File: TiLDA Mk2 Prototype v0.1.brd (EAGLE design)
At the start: 68 x 100 mm, 213 parts, among them IC1 ATSAM3X8EA-AU, IC2 MPU-6050, IC3 SRF-V1.2, IC4 LTC4160, IC5 S25FL216K0PMFI011, IC6 AT45DB161E-SSHFHA (NP), IC7 HMC5883LSMD (NP), IC8 MCP1825T-3302E/DC, J1 FCI 62684-401100ALF, J2 EPD-62684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

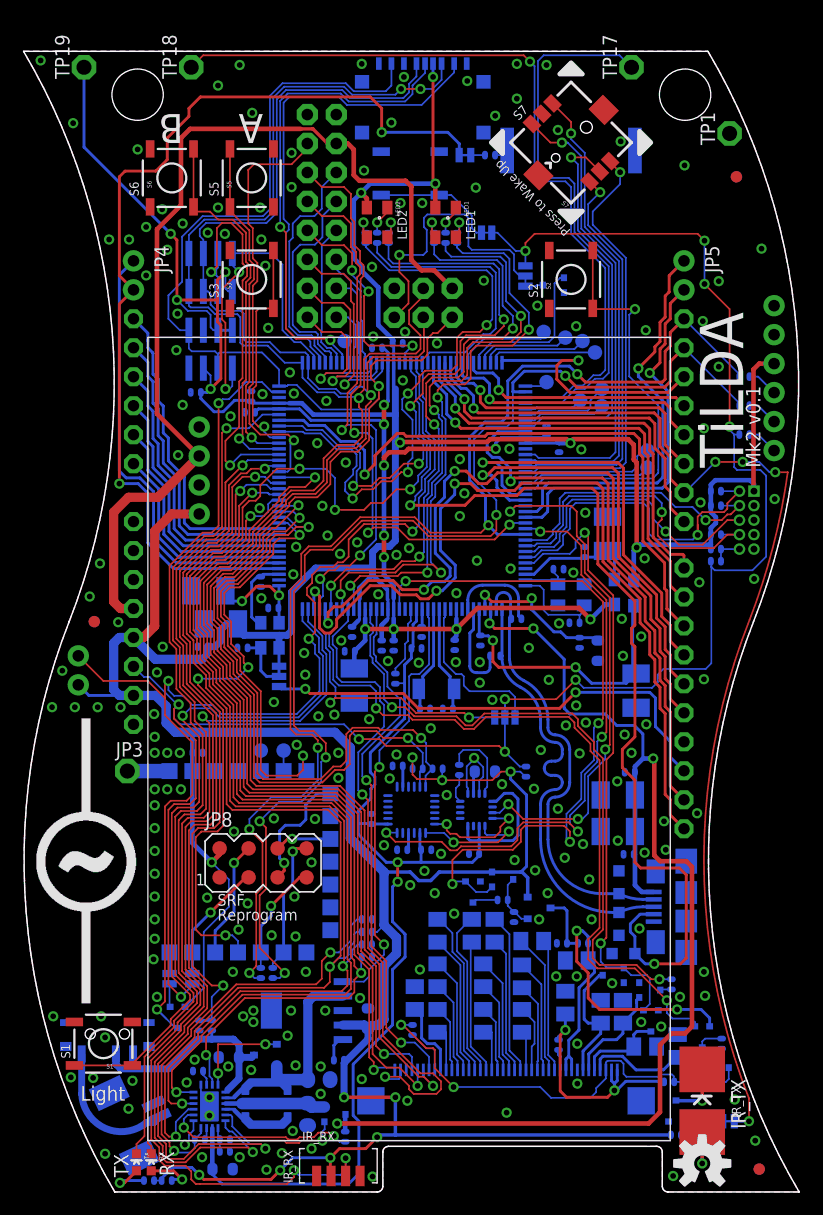
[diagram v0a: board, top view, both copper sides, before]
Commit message: Prototype: Lots of cleaning up, part values, few tracks, Added decoupling for IR TX and FTDI
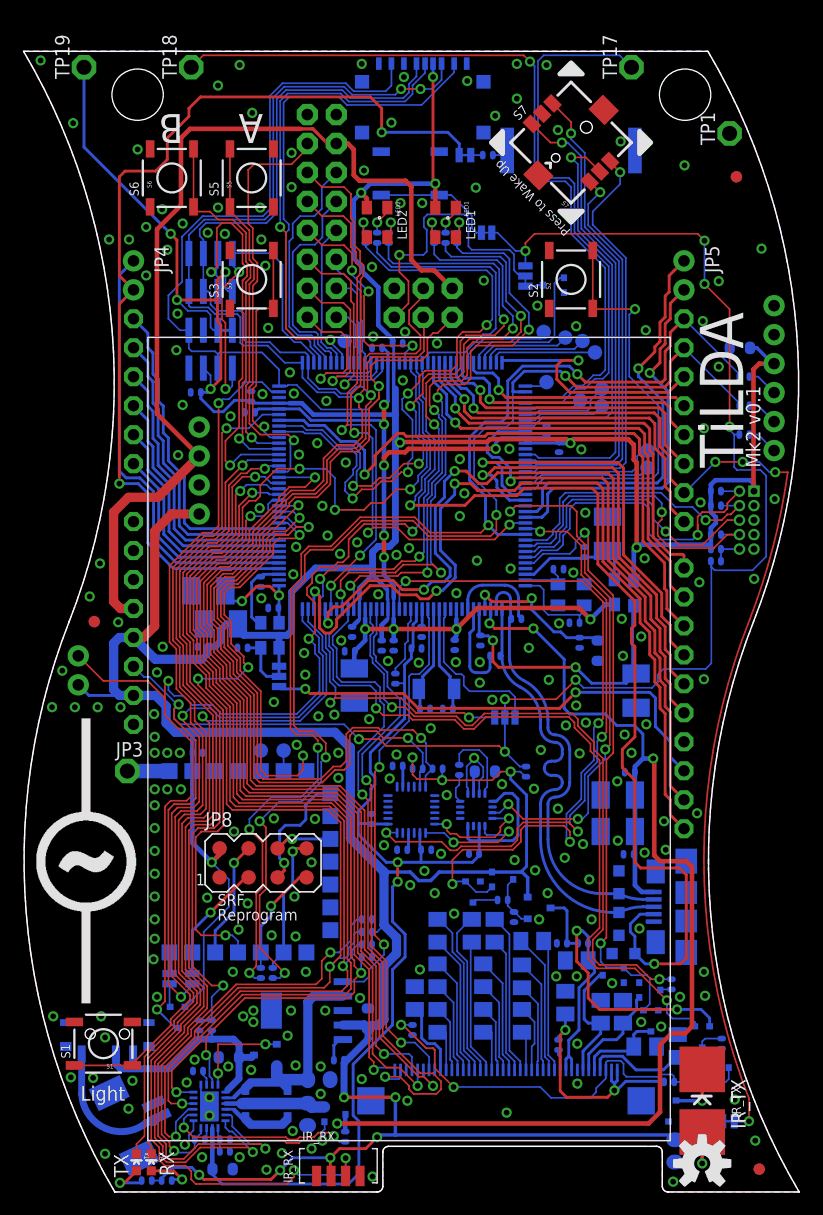
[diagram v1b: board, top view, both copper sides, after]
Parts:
- removed U$2: BATTERY-OUTLINE-55X44, TiLDA Mk2 Parts:BATTERY-55X44
- added C37: 0805/22u/25V/X5R, TiLDA Mk2 Parts:C0805RND
- added C38: 0603/1u/6V/X5R, TiLDA Mk2 Parts:C0603-ROUND
- added OUTINE2: BATTERY-OUTLINE32X50-52X64, TiLDA Mk2 Parts:BATTERY-32X50-52X64
- C104, C105, C106, C107, C108, C109, C110, C112, C113, C114, C115, C116, C117, C118, C119, C132, C134, C2, C27, C29, C32, C9: value 0402/100n/10V/Y5V -> 0402/100n/10V/X5R
- C120: value 0402/10n/10v -> 0402/10n/10v/Y5V
- C22: value 0805/2.2u/25v/y5v -> 0805/2.2u/25V/Y5V
- C26: value 0402/100n/16V/X7R -> 0402/100n/10V/X5R
- C3: value 0402/100n/16V/Y5V -> 0402/100n/10V/X5R
- C31: value 0402/u22/10V/X5R -> 0402/0u22/10V/X5R
- C4: value 0402/100n/4V/X7R -> 0402/100n/10V/X5R
- C6: value 0402/100n/2V/X7R -> 0402/100n/10V/X5R
- J1: value FCI 62684-401100ALF -> ZX62-AB-5PA(11)
- J2: value EPD-62684 -> FCI 62684-401100ALF
- J3: value ARDUINOSPI-REFRENCE -> Arduino Headers
- J5: value 1050270001 -> 1050270001 (NP)
- JP2: value JTAG -> JTAG M50-3500542
- Q12: value FDMA905P -> SI2333DS-T1-E3
- Q8: value BC847BSDM?? -> BSS84W
- R10, R21, R22, R23, R24: value 0402/100K/5% -> 0402/100K/1%
- R102: value 0402/10K -> 0402/10K/5%
- R104: value 0402/100K -> 0402/100K/1%
- R2: value 0402/33K/5%/(NC) -> 0402/33K/5%/(NP)
- R3: value 0402/0R/5%/(NC) -> 0402/0R/5%/(NP)
- RX: value 0603//LED/RED -> 0603/LED/RED
- S1: value Light -> SKQGAKE010
- S2: value Left -> SKQGAKE010
- S3: value Right -> SKQGAKE010
- S4: value Reset -> SKQGAKE010
- S5: value A -> SKQGAKE010
- S6: value B -> SKQGAKE010
- S7: value JOYSTICK_MINI-APLS -> SKRHAAE010
- moved R4 1.80 mm to (59.0, 5.00)
- moved R8 0.20 mm to (10.8, 1.00)
- moved R25 0.20 mm to (40.7, 90.9)
- renumbered U1 to OUTLINE3, U5 to OUTLINE1
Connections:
- net 3V3: now also C37.1, C38.2
- net GND: now also C37.2, C38.1
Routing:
- net 3V3: track 455.5 -> 460.6 mm
- net IR_TX_A: track 6.81 -> 5.31 mm
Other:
- board text added: "C37"
- board text added: "C38"

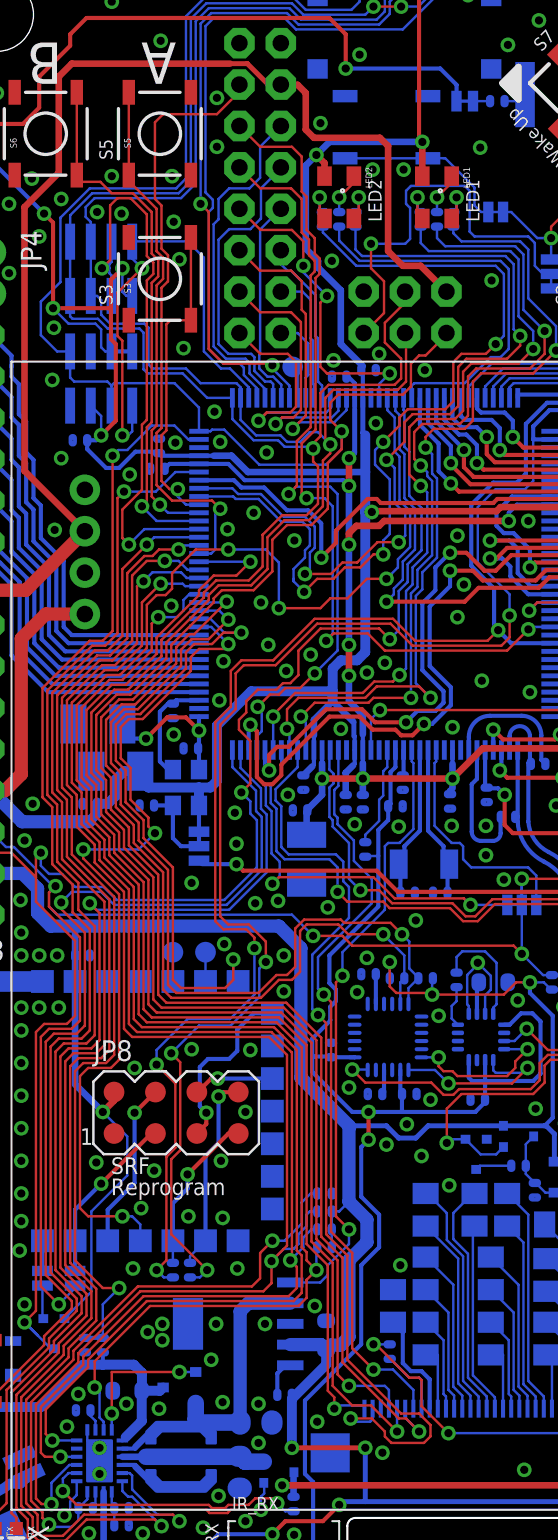
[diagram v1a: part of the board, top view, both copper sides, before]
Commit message: Prototype: swap C30 & C35 for 0805
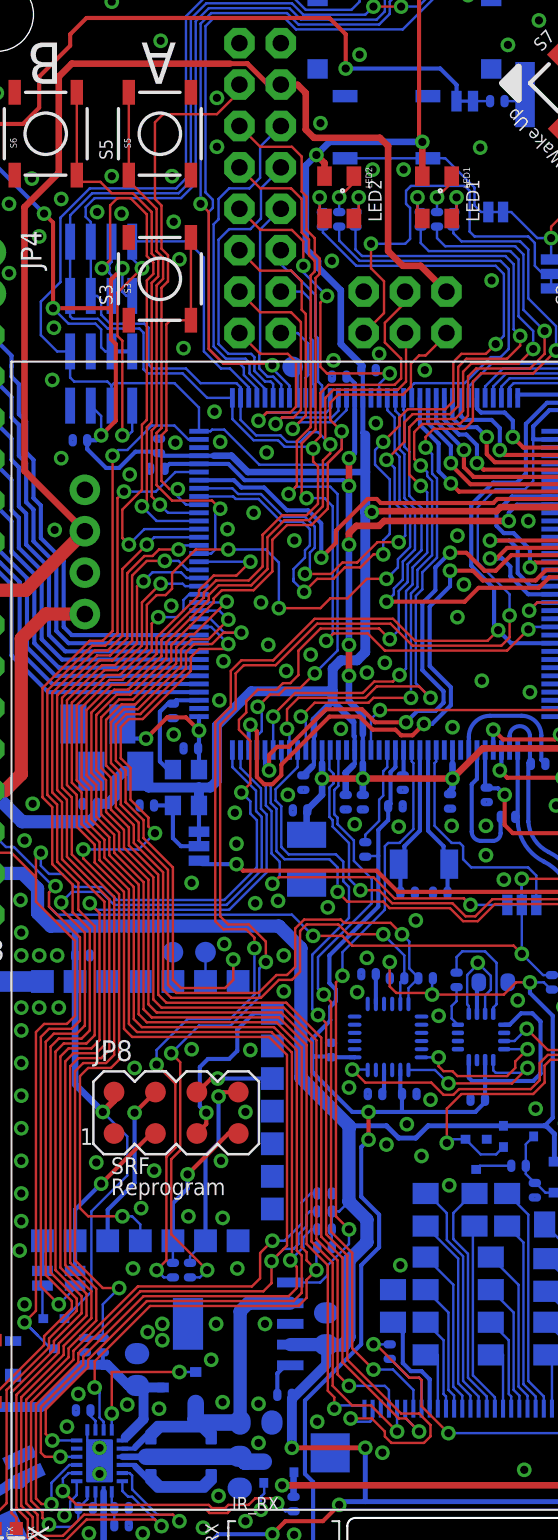
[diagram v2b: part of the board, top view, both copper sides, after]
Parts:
- C30, C35: value 0603/10u/6.3V/X5R -> 0805/10u/6.3V/X5R; device TiLDA Mk2 Parts:C0603-ROUND -> TiLDA Mk2 Parts:C0805RND
- moved C35 1.43 mm to (18.6, 13.1), turned to 270 degrees
- moved C30 0.40 mm to (30.2, 15.6)
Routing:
- net VBATT_SWITCHED: track 19.9 -> 19.4 mm
- net GND: vias 236 -> 235
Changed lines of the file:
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@@
 <setting verticaltext="up"/>
 </settings>
-<grid distance="0.5" unitdist="mm" unit="mm" style="lines" multiple="1" display="yes" altdistance="0.25" altunitdist="mm" altunit="mm"/>
+<grid distance="0.1" unitdist="mm" unit="mm" style="lines" multiple="1" display="yes" altdistance="0.05" altunitdist="mm" altunit="mm"/>
 <layers>
 <layer number="1" name="Top" color="4" fill="1" visible="yes" active="yes"/>
@@
 <layer number="38" name="bTest" color="7" fill="1" visible="no" active="yes"/>
 <layer number="39" name="tKeepout" color="4" fill="11" visible="no" active="yes"/>
-<layer number="40" name="bKeepout" color="1" fill="11" visible="yes" active="yes"/>
+<layer number="40" name="bKeepout" color="1" fill="11" visible="no" active="yes"/>
 <layer number="41" name="tRestrict" color="4" fill="10" visible="no" active="yes"/>
 <layer number="42" name="bRestrict" color="1" fill="10" visible="no" active="yes"/>
@@
 <text x="27.95" y="96.6" size="0.8128" layer="22" ratio="15" rot="MR90">J5</text>
 <text x="10" y="38.2" size="0.8128" layer="22" ratio="15" rot="MR0">ANT</text>
-<text x="19.5" y="12.6" size="0.8128" layer="22" ratio="15" rot="MR90">Q12</text>
+<text x="19.5" y="12.5" size="0.8128" layer="22" ratio="15" rot="MR90">Q12</text>
 <text x="29" y="3.2" size="0.8128" layer="22" ratio="15" rot="MR90">Q11</text>
 <text x="59.7" y="6.6" size="0.8128" layer="22" ratio="15" rot="MR0">Q9</text>
@@
 <text x="20.9" y="1.1" size="0.6096" layer="22" ratio="15" rot="MR0">C34</text>
 <text x="15.4" y="11.9" size="0.6096" layer="22" ratio="15" rot="MR0">R29</text>
-<text x="18.9" y="12.6" size="0.6096" layer="22" ratio="15" rot="MR0">C35</text>
+<text x="17" y="12" size="0.6096" layer="22" ratio="15" rot="MR90">C35</text>
 <text x="24.4" y="3.2" size="0.6096" layer="22" ratio="15" rot="MR90">C33</text>
 <text x="30" y="2.7" size="0.6096" layer="22" ratio="15" rot="MR90">R28</text>
@@
 <text x="26.5" y="10.7" size="0.6096" layer="22" ratio="15" rot="MR0">C36</text>
 <text x="31.1" y="14.4" size="0.6096" layer="22" ratio="15" rot="MR90">C30</text>
-<text x="17.9" y="13.9" size="0.6096" layer="22" ratio="15" rot="MR90">R38</text>
-<text x="17.1" y="13.9" size="0.6096" layer="22" ratio="15" rot="MR90">R39</text>
+<text x="18" y="15.6" size="0.6096" layer="22" ratio="15" rot="MR90">R38</text>
+<text x="17.2" y="15.6" size="0.6096" layer="22" ratio="15" rot="MR90">R39</text>
 <text x="19.8" y="17.3" size="0.6096" layer="22" ratio="15" rot="MR90">R6</text>
 <text x="19" y="17.3" size="0.6096" layer="22" ratio="15" rot="MR90">R5</text>
@@
 <element name="L1" library="TiLDA Mk2 Parts" package="LPS4018" value="LPS4018-332MLB" x="21.3" y="7.75" rot="MR270"/>
 <element name="Q12" library="TiLDA Mk2 Parts" package="SOT23-R" value="SI2333DS-T1-E3" x="21.2" y="12" rot="MR270"/>
-<element name="C35" library="TiLDA Mk2 Parts" package="C0603-ROUND" value="0603/10u/6.3V/X5R" x="18" y="11.8" rot="MR180"/>
+<element name="C35" library="TiLDA Mk2 Parts" package="C0805RND" value="0805/10u/6.3V/X5R" x="18.6" y="13.1" rot="MR270"/>
 <element name="C36" library="TiLDA Mk2 Parts" package="C0805RND" value="0805/22u/25V/X5R" x="25.9" y="9.85" rot="MR0"/>
 <element name="R27" library="TiLDA Mk2 Parts" package="R0402-ARDUINO-ROUND" value="0402/100K/1%" x="15.45" y="4.6" rot="MR180"/>
@@
 <element name="R32" library="TiLDA Mk2 Parts" package="R0402-ARDUINO-ROUND" value="0402/0R/5%" x="63.2" y="71.48" rot="MR0"/>
 <element name="SJ6" library="TiLDA Mk2 Parts" package="SJ_2S-NO" value="RESET BUTTON" x="40.6" y="84.1" rot="MR0"/>
-<element name="C30" library="TiLDA Mk2 Parts" package="C0603-ROUND" value="0603/10u/6.3V/X5R" x="30.2" y="15.2" rot="MR90"/>
+<element name="C30" library="TiLDA Mk2 Parts" package="C0805RND" value="0805/10u/6.3V/X5R" x="30.2" y="15.6" rot="MR90"/>
 <element name="R26" library="TiLDA Mk2 Parts" package="R0402-ARDUINO-ROUND" value="0402/10K/5%" x="27.65" y="11.55" rot="MR180"/>
 <element name="IC6" library="TiLDA Mk2 Parts" package="SO08-EIAJ" value="AT45DB161E-SSHFHA (NP)" x="16.4" y="78.9" rot="MR180"/>
@@
 <via x="26.9" y="3" extent="1-16" drill="0.5"/>
 <contactref element="C30" pad="1"/>
-<wire x1="30.2" y1="14.311" x2="29.881" y2="14.63" width="0.8128" layer="16"/>
 <wire x1="29.881" y1="14.63" x2="28.0004" y2="14.63" width="0.8128" layer="16"/>
 <wire x1="12.1055" y1="1" x2="12.1" y2="1" width="0.254" layer="16"/>
@@
 <wire x1="30" y1="3.8" x2="31" y2="4.8" width="0.254" layer="1"/>
 <via x="31" y="4.8" extent="1-16" drill="0.5"/>
-<wire x1="30.2" y1="14.311" x2="30.489" y2="14.6" width="0.8128" layer="16"/>
-<wire x1="30.489" y1="14.6" x2="31.1" y2="14.6" width="0.8128" layer="16"/>
-<wire x1="31.1" y1="14.6" x2="31.6" y2="15.1" width="0.8128" layer="16"/>
+<wire x1="30.689" y1="14.6" x2="30.7" y2="14.6" width="0.8128" layer="16"/>
+<wire x1="30.7" y1="14.6" x2="31.3" y2="14.6" width="0.8128" layer="16"/>
+<wire x1="31.3" y1="14.6" x2="31.6" y2="15.1" width="0.8128" layer="16"/>
 <wire x1="31.6" y1="15.1" x2="31.6" y2="19.8" width="0.8128" layer="16"/>
 <wire x1="31.6" y1="19.8" x2="32.7" y2="20.9" width="0.8128" layer="16"/>
@@
 <wire x1="34.65" y1="27.3" x2="33.9" y2="28.05" width="0.3048" layer="16"/>
 <wire x1="33.9" y1="28.05" x2="31.6" y2="28.05" width="0.3048" layer="16"/>
-<wire x1="30.2" y1="14.311" x2="30.2" y2="13.4" width="0.6096" layer="16"/>
+<wire x1="30.2" y1="14.623" x2="30.2" y2="13.4" width="0.6096" layer="16"/>
 <wire x1="30.2" y1="13.4" x2="28.1" y2="11.3" width="0.6096" layer="16"/>
 <wire x1="28.1" y1="11.3" x2="28.1" y2="8.3" width="0.6096" layer="16"/>
@@
 <wire x1="64.3" y1="74" x2="65.68" y2="72.62" width="0.3084" layer="16"/>
 <wire x1="65.68" y1="72.62" x2="65.8" y2="72.62" width="0.3084" layer="16"/>
+<wire x1="30.2" y1="14.623" x2="30.7" y2="14.623" width="0.4064" layer="16"/>
+<wire x1="30.7" y1="14.623" x2="30.7" y2="14.6" width="0.4064" layer="16"/>
+<wire x1="30.2" y1="14.623" x2="29.881" y2="14.623" width="0.4064" layer="16"/>
+<wire x1="29.881" y1="14.623" x2="29.881" y2="14.63" width="0.4064" layer="16"/>
 </signal>
 <signal name="GND">
@@
 <via x="20.95" y="69.95" extent="1-16" drill="0.5"/>
 <via x="20.75" y="86.3" extent="1-16" drill="0.5"/>
-<via x="17.95" y="11" extent="1-16" drill="0.5"/>
+<via x="18" y="10.95" extent="1-16" drill="0.5"/>
 <via x="15" y="11.6" extent="1-16" drill="0.5"/>
 <via x="16.1" y="25.8" extent="1-16" drill="0.5"/>
@@
 <via x="19.25" y="15.4" extent="1-16" drill="0.5"/>
 <via x="26.45" y="15.9" extent="1-16" drill="0.5"/>
-<via x="29.5" y="17" extent="1-16" drill="0.5"/>
 <via x="23.45" y="15.9" extent="1-16" drill="0.5"/>
 <via x="19.95" y="10.7" extent="1-16" drill="0.5"/>
@@
 <wire x1="37.2" y1="92.9" x2="38.2" y2="91.9" width="0.254" layer="16"/>
 <wire x1="38.2" y1="91.9" x2="38.2" y2="90.9" width="0.254" layer="16"/>
-<wire x1="38.2" y1="90.9" x2="38.192" y2="90.9" width="0" layer="19" extent="16-16"/>
+<wire x1="38.192" y1="90.9" x2="38.2" y2="90.9" width="0.4064" layer="16"/>
 </signal>
 <signal name="UOTGVBOF">
@@
 <contactref element="C35" pad="2"/>
 <wire x1="17.7" y1="8.75" x2="17.9" y2="8.95" width="0.254" layer="16"/>
-<wire x1="17.9" y1="8.95" x2="18.889" y2="9.939" width="0.6096" layer="16"/>
-<wire x1="18.889" y1="9.939" x2="18.889" y2="11.8" width="0.6096" layer="16"/>
-<wire x1="20.2" y1="12" x2="20" y2="11.8" width="0.6096" layer="16"/>
-<wire x1="20" y1="11.8" x2="18.889" y2="11.8" width="0.6096" layer="16"/>
+<wire x1="17.9" y1="8.95" x2="19" y2="10.05" width="0.6096" layer="16"/>
+<wire x1="19" y1="10.05" x2="19" y2="12" width="0.6096" layer="16"/>
+<wire x1="20.2" y1="12" x2="19" y2="12" width="0.6096" layer="16"/>
+<wire x1="19" y1="12" x2="18.6" y2="12" width="0.6096" layer="16"/>
+<wire x1="18.6" y1="12" x2="18.6" y2="12.123" width="0.6096" layer="16"/>
 <wire x1="15.3" y1="13.4" x2="16.5" y2="13.4" width="0.6096" layer="16"/>
-<wire x1="16.5" y1="13.4" x2="18.4" y2="13.4" width="0.6096" layer="16"/>
-<wire x1="18.4" y1="13.4" x2="18.9" y2="12.9" width="0.6096" layer="16"/>
-<wire x1="18.9" y1="12.9" x2="18.9" y2="11.811" width="0.6096" layer="16"/>
-<wire x1="18.9" y1="11.811" x2="18.889" y2="11.8" width="0.6096" layer="16"/>
+<wire x1="16.5" y1="13.4" x2="16.773" y2="13.4" width="0.6096" layer="16"/>
+<wire x1="16.773" y1="13.4" x2="18.05" y2="12.123" width="0.6096" layer="16"/>
+<wire x1="18.05" y1="12.123" x2="18.6" y2="12.123" width="0.6096" layer="16"/>
 <contactref element="R38" pad="2"/>
 <wire x1="16.5" y1="14.1555" x2="16.5" y2="13.4" width="0.254" layer="16"/>
